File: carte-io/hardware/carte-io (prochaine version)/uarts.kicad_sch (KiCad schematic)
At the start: 15 parts, among them J18 JST_PH_B4B, J19 JST_PH_B4B, J27 JST_PH_B5B, U20 74LVC2G125DP,125, U21 CM1293A-04SO, U26 74LVC2G125DP,125, U27 CM1293A-04SO, U28 74LVC2G125DP,125, U29 CM1293A-04SO

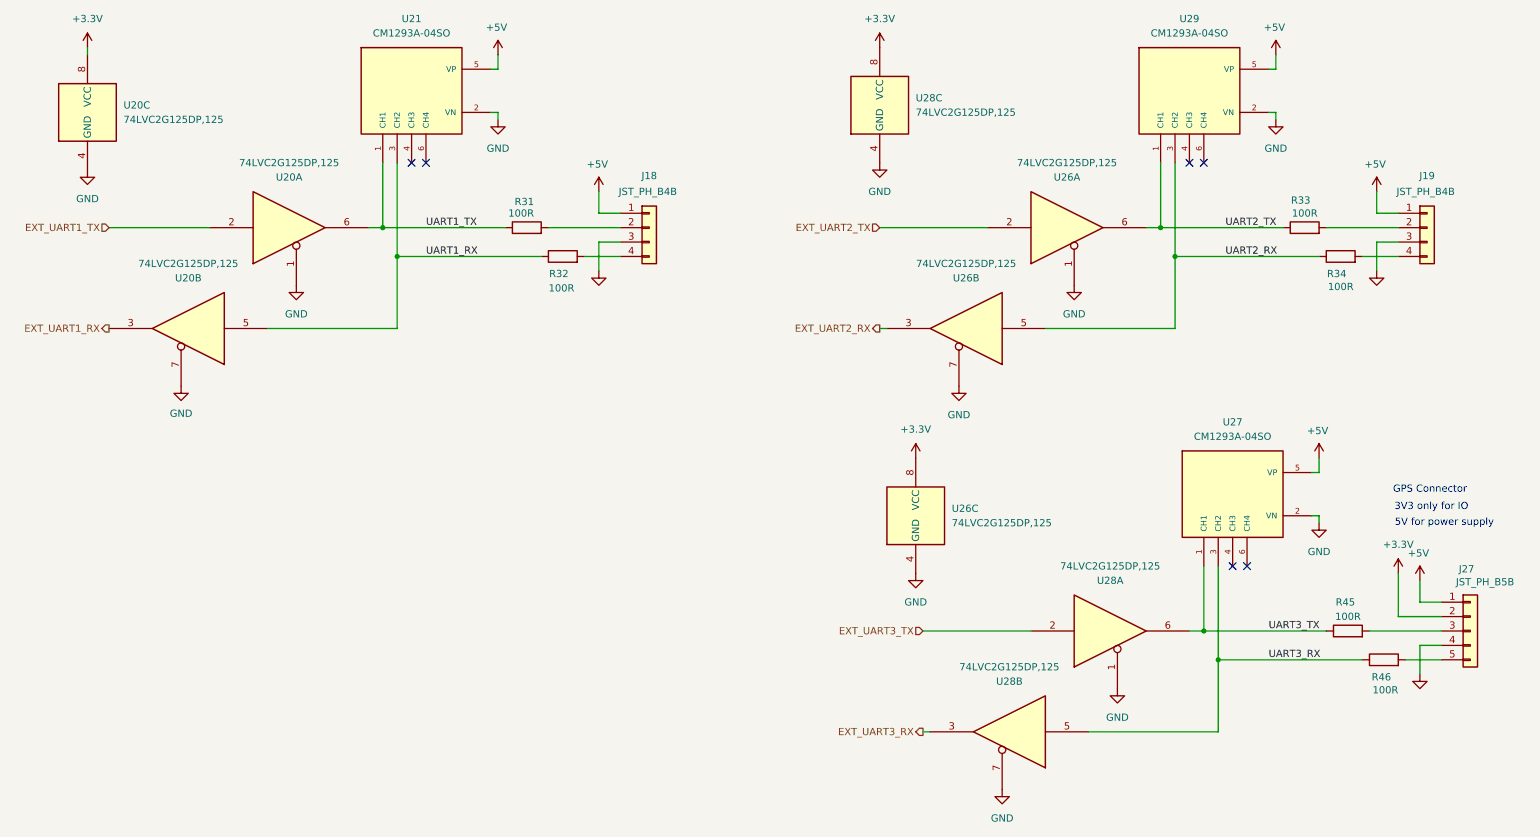
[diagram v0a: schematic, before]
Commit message: Commit de sauvegarde, gros changement sur la carte IO, les connecteurs sont compatibles SeeedStudio Grove. Il faut reprendre une grosse partie du routage et rajouter deux entrées analogiques
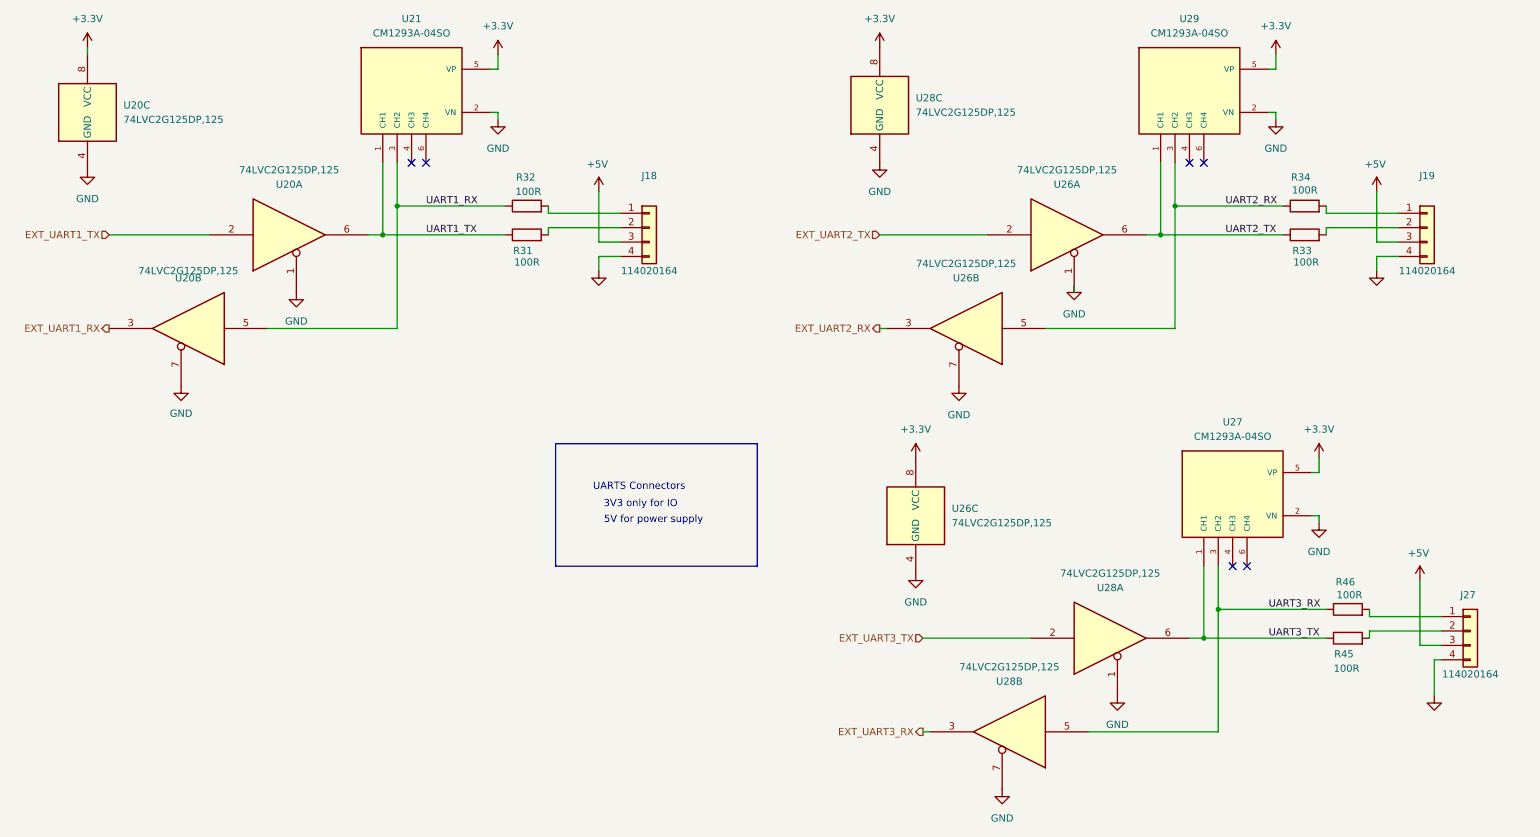
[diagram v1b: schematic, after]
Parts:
- J18, J19: value JST_PH_B4B -> 114020164; footprint Connector_JST:JST_PH_B4B-PH-K_1x04_P2.00mm_Vertical -> SeeedStudio - Horizontal Header -114020164:SEEEDSTUDIO_114020164; symbol Connector_Generic:Conn_01x04 -> SeeedStudio - Horizontal header:SeeedStudio - 114020164 - R/A
- J27: value JST_PH_B5B -> 114020164; footprint Connector_JST:JST_PH_B5B-PH-K_1x05_P2.00mm_Vertical -> SeeedStudio - Horizontal Header -114020164:SEEEDSTUDIO_114020164; symbol Connector_Generic:Conn_01x05 -> SeeedStudio - Horizontal header:SeeedStudio - 114020164 - R/A
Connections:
- net +3.3V: now also U21.5 (VP), U27.5 (VP), U29.5 (VP); no longer J27.2 (Pin_2)
- net +5V: now also J18.3 (Pin_3), J19.3 (Pin_3), J27.3 (Pin_3); no longer J18.1 (Pin_1), J19.1 (Pin_1), J27.1 (Pin_1), U21.5 (VP), U27.5 (VP), U29.5 (VP)
- net GND: now also J18.4 (Pin_4), J19.4 (Pin_4); no longer J18.3 (Pin_3), J19.3 (Pin_3)
- net at R34.2: now also J19.1 (Pin_1); no longer J19.4 (Pin_4)
- net at R45.2: now also J27.2 (Pin_2); no longer J27.3 (Pin_3)
- net at R32.2: now also J18.1 (Pin_1); no longer J18.4 (Pin_4)
- net at R46.2: now also J27.1 (Pin_1); no longer J27.5 (Pin_5)
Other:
- note added: "UARTS Connectors"
- note removed: "GPS Connector"
- moved on the sheet: R31, R32, R33, R34, R45, R46, U20A, U26A, U28A

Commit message: -- reorganisation de la carte, - rajout des connecteurs seeedstudio grove - Rajout des deux entrées ADC
travail en cours
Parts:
- U20, U26, U28: footprint Package_SO:VSSOP-8_2.3x2mm_P0.5mm -> Package_SO:TSSOP-8_3x3mm_P0.65mm
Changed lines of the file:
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@@
 			)
 		)
-		(property "Footprint" "Package_SO:VSSOP-8_2.3x2mm_P0.5mm"
+		(property "Footprint" "Package_SO:TSSOP-8_3x3mm_P0.65mm"
 			(at 193.04 142.24 0)
 			(effects
@@
 			)
 		)
-		(property "Footprint" "Package_SO:VSSOP-8_2.3x2mm_P0.5mm"
+		(property "Footprint" "Package_SO:TSSOP-8_3x3mm_P0.65mm"
 			(at 177.8 104.14 0)
 			(effects
@@
 			)
 		)
-		(property "Footprint" "Package_SO:VSSOP-8_2.3x2mm_P0.5mm"
+		(property "Footprint" "Package_SO:TSSOP-8_3x3mm_P0.65mm"
 			(at 48.26 71.12 0)
 			(effects
@@
 			)
 		)
-		(property "Footprint" "Package_SO:VSSOP-8_2.3x2mm_P0.5mm"
+		(property "Footprint" "Package_SO:TSSOP-8_3x3mm_P0.65mm"
 			(at 171.45 31.75 0)
 			(effects
@@
 			)
 		)
-		(property "Footprint" "Package_SO:VSSOP-8_2.3x2mm_P0.5mm"
+		(property "Footprint" "Package_SO:TSSOP-8_3x3mm_P0.65mm"
 			(at 185.42 71.12 0)
 			(effects
@@
 			)
 		)
-		(property "Footprint" "Package_SO:VSSOP-8_2.3x2mm_P0.5mm"
+		(property "Footprint" "Package_SO:TSSOP-8_3x3mm_P0.65mm"
 			(at 68.58 54.61 0)
 			(effects
@@
 			)
 		)
-		(property "Footprint" "Package_SO:VSSOP-8_2.3x2mm_P0.5mm"
+		(property "Footprint" "Package_SO:TSSOP-8_3x3mm_P0.65mm"
 			(at 213.36 125.73 0)
 			(effects
@@
 			)
 		)
-		(property "Footprint" "Package_SO:VSSOP-8_2.3x2mm_P0.5mm"
+		(property "Footprint" "Package_SO:TSSOP-8_3x3mm_P0.65mm"
 			(at 31.75 33.02 0)
 			(effects
@@
 			)
 		)
-		(property "Footprint" "Package_SO:VSSOP-8_2.3x2mm_P0.5mm"
+		(property "Footprint" "Package_SO:TSSOP-8_3x3mm_P0.65mm"
 			(at 205.74 54.61 0)
 			(effects
